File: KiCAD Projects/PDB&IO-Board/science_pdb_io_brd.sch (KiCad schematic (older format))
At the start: 21 parts, among them P1 ROBOT_PWR_IN, P12 ENCODER_2, P13 LIMIT1_IN, P14 LIMIT2_IN, P15 LIMIT3_IN, P16 ENCODER_3, P17 MOTOR1_PWM, P18 MOTOR2_PWM, P19 MOTOR3_PWM, P2 12V-5V_REG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

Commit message: More schematic work
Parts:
- added C? (x3): C, symbol C
- added R? (x3): R, symbol R
- added U?: SN74HC14N, symbol SN74HC14N
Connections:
- net +5V: now also R?.1, R?.1, R?.1, U?.14 (Vcc)
- net GND: now also C?.2, C?.2, C?.2, U?.7 (GND)
- net LIMIT1_IN: now also U?.2 (1Y); no longer P13.2 (P2)
- net LIMIT2_IN: now also U?.4; no longer P14.2 (P2)
- net LIMIT3_IN: now also U?.6 (3Y); no longer P15.2 (P2)
- new net B_LIM1: C?.1, P13.2 (P2), R?.2, U?.1 (1A)
- new net B_LIM2: C?.1, P14.2 (P2), R?.2, U?.3 (2A)
- new net B_LIM3: C?.1, P15.2 (P2), R?.2, U?.5 (3A)
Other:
- moved on the sheet: P13, P14, P15, P17, P18, P19, P20

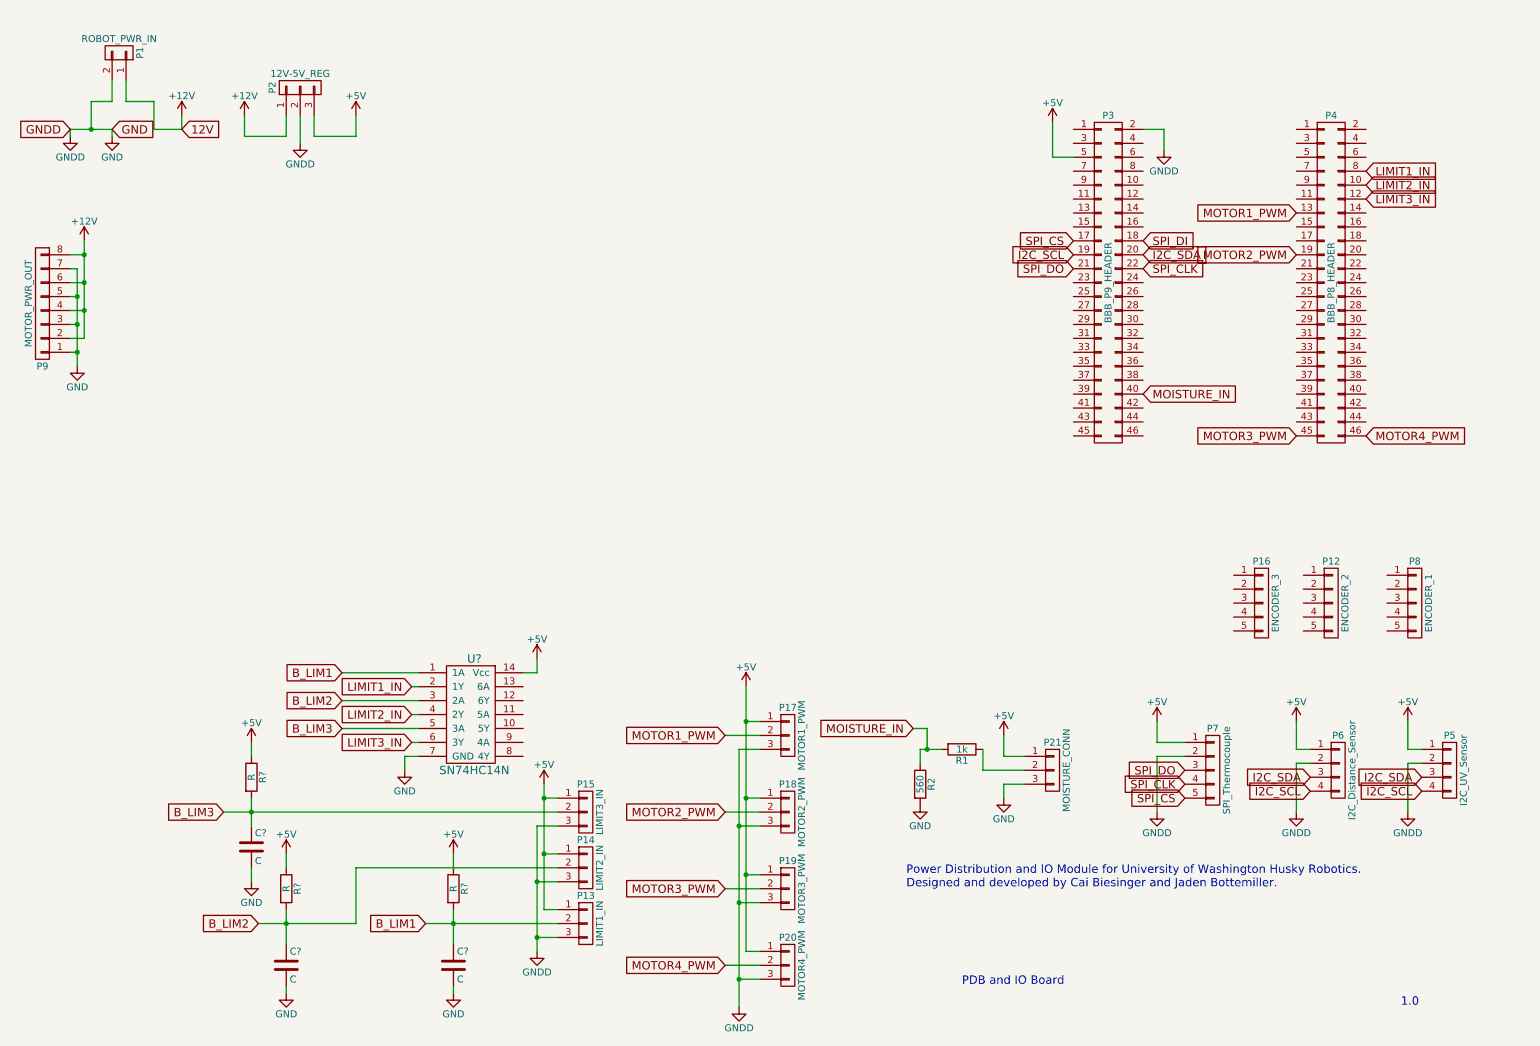
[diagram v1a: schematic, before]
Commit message: Minor Schematic Tweaks
No functional changes, just making the schematic look a little nicer.
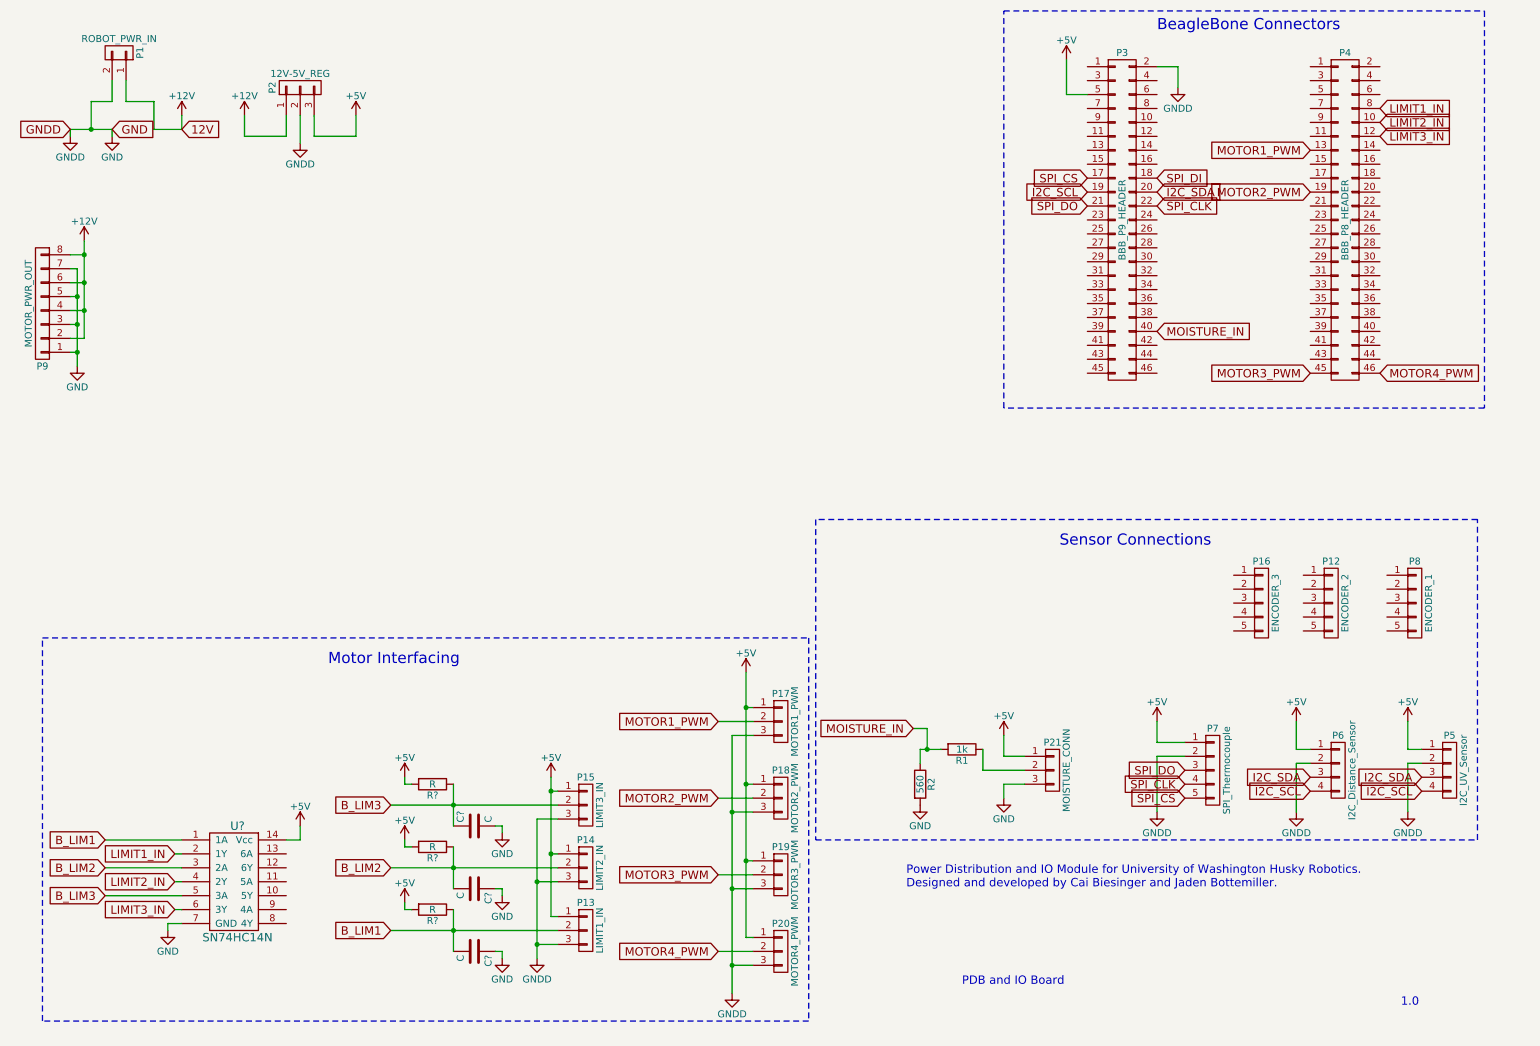
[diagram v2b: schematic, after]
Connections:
- net +5V: now also R?.2, R?.2, R?.2; no longer R?.1, R?.1, R?.1
- net B_LIM1: now also C?.2, R?.1; no longer C?.1, R?.2
- net B_LIM2: now also C?.2, R?.1; no longer C?.1, R?.2
- net B_LIM3: now also R?.1; no longer R?.2
- net GND: now also C?.1, C?.1; no longer C?.2, C?.2
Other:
- note added: "BeagleBone Connectors"
- note added: "Motor Interfacing"
- note added: "Sensor Connections"
- moved on the sheet: C?, P13, P15, P17, P18, P19, P20, P3, P4, R?, U?

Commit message: Board updates
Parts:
- added P?: BB_Power, symbol CONN_01X02
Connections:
- net +5V: now also P?.2 (P2); no longer P3.5 (P5)
- net GND: now also P?.1 (P1); no longer P3.2 (P2)
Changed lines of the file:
@@
 	1    0    0    -1
 $EndComp
-Text GLabel 1050 1350 0    60   Input ~ 0
-GNDD
-Text GLabel 1350 1350 2    60   Input ~ 0
-GND
 $Comp
 L +12V #PWR5
@@
 	1    0    0    -1
 $EndComp
-Text GLabel 1850 1350 2    60   Input ~ 0
-12V
 $Comp
 L CONN_01X02 P1
@@
 	1    0    0    -1
 $EndComp
-$Comp
-L +5V #PWR16
-U 1 1 5891B3C4
-P 8200 850
-F 0 "#PWR16" H 8200 700 50  0001 C CNN
-F 1 "+5V" H 8200 990 50  0000 C CNN
-F 2 "" H 8200 850 50  0000 C CNN
-F 3 "" H 8200 850 50  0000 C CNN
-	1    8200 850
-	1    0    0    -1
-$EndComp
-$Comp
-L GNDD #PWR19
-U 1 1 5891B4A8
-P 9000 1050
-F 0 "#PWR19" H 9000 800 50  0001 C CNN
-F 1 "GNDD" H 9000 900 50  0000 C CNN
-F 2 "" H 9000 1050 50  0000 C CNN
-F 3 "" H 9000 1050 50  0000 C CNN
-	1    9000 1050
-	1    0    0    -1
-$EndComp
 Text GLabel 10450 1200 2    60   Input ~ 0
 LIMIT1_IN
@@
 	7150 5800 7150 5900
 Wire Wire Line
-	7150 5800 7300 5800
+	7150 5800 7200 5800
+Wire Wire Line
+	7200 5800 7300 5800
 Wire Wire Line
 	7600 5950 7900 5950
@@
 	5800 5700 5950 5700
 Wire Wire Line
-	5800 5700 5800 7550
+	5800 5700 5800 6250
+Wire Wire Line
+	5800 6250 5800 6800
+Wire Wire Line
+	5800 6800 5800 7350
+Wire Wire Line
+	5800 7350 5800 7550
 Wire Wire Line
 	5900 7150 5950 7150
 Wire Wire Line
-	5900 5250 5900 7150
-Wire Wire Line
-	9000 900  9000 1050
-Wire Wire Line
-	8850 900  9000 900
-Wire Wire Line
-	8200 1100 8350 1100
-Wire Wire Line
-	8200 850  8200 1100
-Wire Wire Line
-	3350 6200 4550 6200
-Wire Wire Line
-	3350 7100 4550 7100
+	5900 5250 5900 5500
+Wire Wire Line
+	5900 5500 5900 6050
+Wire Wire Line
+	5900 6050 5900 6600
+Wire Wire Line
+	5900 6600 5900 7150
+Wire Wire Line
+	3350 6200 3800 6200
+Wire Wire Line
+	3800 6200 4550 6200
+Wire Wire Line
+	3350 7100 3800 7100
+Wire Wire Line
+	3800 7100 4550 7100
 Connection ~ 4400 7200
 Wire Wire Line
@@
 	4500 7000 4550 7000
 Wire Wire Line
-	4500 6000 4500 7000
+	4500 6000 4500 6100
+Wire Wire Line
+	4500 6100 4500 6550
+Wire Wire Line
+	4500 6550 4500 7000
 Wire Wire Line
 	4400 6300 4550 6300
 Wire Wire Line
-	4400 6300 4400 7300
+	4400 6300 4400 6750
+Wire Wire Line
+	4400 6750 4400 7200
+Wire Wire Line
+	4400 7200 4400 7300
 Connection ~ 1150 2450
 Wire Wire Line
@@
 	1150 2850 1050 2850
 Wire Wire Line
-	1150 2150 1150 2850
+	1150 2150 1150 2250
+Wire Wire Line
+	1150 2250 1150 2450
+Wire Wire Line
+	1150 2450 1150 2650
+Wire Wire Line
+	1150 2650 1150 2850
 Wire Wire Line
 	1050 2250 1150 2250
@@
 	1050 2550 1100 2550
 Wire Wire Line
-	1100 2350 1100 3050
+	1100 2350 1100 2550
+Wire Wire Line
+	1100 2550 1100 2750
+Wire Wire Line
+	1100 2750 1100 2950
+Wire Wire Line
+	1100 2950 1100 3050
 Wire Wire Line
 	1050 2350 1100 2350
@@
 	1350 1350 1350 1400
 Wire Wire Line
-	1050 1350 1350 1350
+	1050 1350 1200 1350
+Wire Wire Line
+	1200 1350 1350 1350
 Wire Wire Line
 	1050 1400 1050 1350
@@
 $EndComp
 Wire Wire Line
-	3800 6500 3800 6800
+	3800 6500 3800 6650
+Wire Wire Line
+	3800 6650 3800 6800
 $Comp
 L R R?
@@
 $EndComp
 Wire Wire Line
-	3800 6950 3800 7250
+	3800 6950 3800 7100
+Wire Wire Line
+	3800 7100 3800 7250
 $Comp
 L C C?
@@
 	4150 6800 4100 6800
 Wire Wire Line
-	3350 6650 4550 6650
+	3350 6650 3800 6650
+Wire Wire Line
+	3800 6650 4550 6650
 Connection ~ 3800 6650
 Wire Wire Line
-	3800 6050 3800 6350
+	3800 6050 3800 6200
+Wire Wire Line
+	3800 6200 3800 6350
 Wire Wire Line
 	4150 6400 4150 6350
@@
 Text Notes 2900 5200 0    80   ~ 0
 Motor Interfacing
+$Comp
+L CONN_01X02 P?
+U 1 1 58A8DADF
+P 1600 2000
+F 0 "P?" H 1600 2150 50  0000 C CNN
+F 1 "BB_Power" V 1700 2000 50  0000 C CNN
+F 2 "" H 1600 2000 50  0000 C CNN
+F 3 "" H 1600 2000 50  0000 C CNN
+	1    1600 2000
+	-1   0    0    1
+$EndComp
+Wire Wire Line
+	1800 1950 1900 1950
+Wire Wire Line
+	1900 1950 1900 1850
+Wire Wire Line
+	1800 2050 1900 2050
+Wire Wire Line
+	1900 2050 1900 2150
+$Comp
+L +5V #PWR?
+U 1 1 58A8EB99
+P 1900 1850
+F 0 "#PWR?" H 1900 1700 50  0001 C CNN
+F 1 "+5V" H 1900 1990 50  0000 C CNN
+F 2 "" H 1900 1850 50  0000 C CNN
+F 3 "" H 1900 1850 50  0000 C CNN
+	1    1900 1850
+	1    0    0    -1
+$EndComp
+$Comp
+L GNDD #PWR?
+U 1 1 58A8EBE7
+P 1900 2150
+F 0 "#PWR?" H 1900 1900 50  0001 C CNN
+F 1 "GNDD" H 1900 2000 50  0000 C CNN
+F 2 "" H 1900 2150 50  0000 C CNN
+F 3 "" H 1900 2150 50  0000 C CNN
+	1    1900 2150
+	1    0    0    -1
+$EndComp
 $EndSCHEMATC

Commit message: Fixed pinouts, started board layout.
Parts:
- removed P5: I2C_UV_Sensor, symbol CONN_01X04
- removed P6: I2C_Distance_Sensor, symbol CONN_01X04
- removed P7: SPI_Thermocouple, symbol CONN_01X05
- added P?: CONN_01X07, symbol CONN_01X07
- added P?: CONN_01X05, symbol CONN_01X05
- added P?: CONN_01X06, symbol CONN_01X06
- gave numbers to parts that had none: 8
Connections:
- net +5V: now also P?.1 (P1), P?.1 (P1), P?.2 (P2)
- net GND: now also P3.1 (P1), P3.2 (P2), P3.43 (P43), P3.44 (P44), P3.45 (P45), P3.46 (P46), P4.1 (P1), P4.2 (P2), P?.2 (P2), P?.3 (P3), P?.3 (P3); no longer P21.3 (P3), R2.2
- net I2C_SCL: now also P?.3 (P3), P?.5 (P5)
- net I2C_SDA: now also P?.4 (P4), P?.4 (P4)
- net SPI_CLK: now also P?.6 (P6)
- net SPI_CS: now also P?.5 (P5)
- net SPI_DO: now also P?.4 (P4)
- net GNDA: now reaches P3.34 (P34)
- net GNDA: now also P21.3 (P3), R2.2
- no-connect marks 0 -> 5
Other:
- moved on the sheet: R2

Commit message: Worked on PCB
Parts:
- P3, P4: footprint (none) -> Pin_Headers:Pin_Header_Straight_2x23_Pitch2.54mm
- P5: renamed from P?; footprint (none) -> Pin_Headers:Pin_Header_Straight_1x06_Pitch2.54mm
- P6: renamed from P?; footprint (none) -> Pin_Headers:Pin_Header_Straight_1x07_Pitch2.54mm
- P7: renamed from P?; footprint (none) -> Pin_Headers:Pin_Header_Straight_1x05_Pitch2.54mm
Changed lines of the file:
@@
 F 0 "P1" H 1400 950 50  0000 C CNN
 F 1 "ROBOT_PWR_IN" V 1500 800 50  0000 C CNN
-F 2 "" H 1400 800 50  0000 C CNN
+F 2 "" H 1400 800 50  0001 C CNN
 F 3 "" H 1400 800 50  0000 C CNN
 	1    1400 800
@@
 F 0 "P2" H 2700 1250 50  0000 C CNN
 F 1 "12V-5V_REG" V 2800 1050 50  0000 C CNN
-F 2 "" H 2700 1050 50  0000 C CNN
+F 2 "" H 2700 1050 50  0001 C CNN
 F 3 "" H 2700 1050 50  0000 C CNN
 	1    2700 1050
@@
 F 0 "P3" H 8600 3200 50  0000 C CNN
 F 1 "BBB_P9_HEADER" V 8600 2000 50  0000 C CNN
-F 2 "" H 8600 1150 50  0000 C CNN
+F 2 "Pin_Headers:Pin_Header_Straight_2x23_Pitch2.54mm" H 8600 1150 50  0001 C CNN
 F 3 "" H 8600 1150 50  0000 C CNN
 	1    8600 2000
@@
 F 0 "P4" H 10200 3200 50  0000 C CNN
 F 1 "BBB_P8_HEADER" V 10200 2000 50  0000 C CNN
-F 2 "" H 10200 1150 50  0000 C CNN
+F 2 "Pin_Headers:Pin_Header_Straight_2x23_Pitch2.54mm" H 10200 1150 50  0001 C CNN
 F 3 "" H 10200 1150 50  0000 C CNN
 	1    10200 2000
@@
 F 0 "P9" H 850 3050 50  0000 C CNN
 F 1 "MOTOR_PWR_OUT" V 950 2600 50  0000 C CNN
-F 2 "" H 850 2600 50  0000 C CNN
+F 2 "" H 850 2600 50  0001 C CNN
 F 3 "" H 850 2600 50  0000 C CNN
 	1    850  2600
@@
 F 0 "P8" H 10700 5050 50  0000 C CNN
 F 1 "ENCODER_1" V 10800 4750 50  0000 C CNN
-F 2 "" H 10700 4750 50  0000 C CNN
+F 2 "" H 10700 4750 50  0001 C CNN
 F 3 "" H 10700 4750 50  0000 C CNN
 	1    10700 4750
@@
 F 0 "P12" H 10100 5050 50  0000 C CNN
 F 1 "ENCODER_2" V 10200 4750 50  0000 C CNN
-F 2 "" H 10100 4750 50  0000 C CNN
+F 2 "" H 10100 4750 50  0001 C CNN
 F 3 "" H 10100 4750 50  0000 C CNN
 	1    10100 4750
@@
 F 0 "P15" H 4750 6400 50  0000 C CNN
 F 1 "LIMIT3_IN" V 4850 6200 50  0000 C CNN
-F 2 "" H 4750 6200 50  0000 C CNN
+F 2 "" H 4750 6200 50  0001 C CNN
 F 3 "" H 4750 6200 50  0000 C CNN
 	1    4750 6200
@@
 F 0 "P14" H 4750 6850 50  0000 C CNN
 F 1 "LIMIT2_IN" V 4850 6650 50  0000 C CNN
-F 2 "" H 4750 6650 50  0000 C CNN
+F 2 "" H 4750 6650 50  0001 C CNN
 F 3 "" H 4750 6650 50  0000 C CNN
 	1    4750 6650
@@
 F 0 "P13" H 4750 7300 50  0000 C CNN
 F 1 "LIMIT1_IN" V 4850 7100 50  0000 C CNN
-F 2 "" H 4750 7100 50  0000 C CNN
+F 2 "" H 4750 7100 50  0001 C CNN
 F 3 "" H 4750 7100 50  0000 C CNN
 	1    4750 7100
@@
 F 0 "P16" H 9600 5050 50  0000 C CNN
 F 1 "ENCODER_3" V 9700 4750 50  0000 C CNN
-F 2 "" H 9600 4750 50  0000 C CNN
+F 2 "" H 9600 4750 50  0001 C CNN
 F 3 "" H 9600 4750 50  0000 C CNN
 	1    9600 4750
@@
 F 0 "P20" H 6150 7450 50  0000 C CNN
 F 1 "MOTOR4_PWM" V 6250 7250 50  0000 C CNN
-F 2 "" H 6150 7250 50  0000 C CNN
+F 2 "" H 6150 7250 50  0001 C CNN
 F 3 "" H 6150 7250 50  0000 C CNN
 	1    6150 7250
@@
 F 0 "P19" H 6150 6900 50  0000 C CNN
 F 1 "MOTOR3_PWM" V 6250 6700 50  0000 C CNN
-F 2 "" H 6150 6700 50  0000 C CNN
+F 2 "" H 6150 6700 50  0001 C CNN
 F 3 "" H 6150 6700 50  0000 C CNN
 	1    6150 6700
@@
 F 0 "P18" H 6150 6350 50  0000 C CNN
 F 1 "MOTOR2_PWM" V 6250 6150 50  0000 C CNN
-F 2 "" H 6150 6150 50  0000 C CNN
+F 2 "" H 6150 6150 50  0001 C CNN
 F 3 "" H 6150 6150 50  0000 C CNN
 	1    6150 6150
@@
 F 0 "P17" H 6150 5800 50  0000 C CNN
 F 1 "MOTOR1_PWM" V 6250 5600 50  0000 C CNN
-F 2 "" H 6150 5600 50  0000 C CNN
+F 2 "" H 6150 5600 50  0001 C CNN
 F 3 "" H 6150 5600 50  0000 C CNN
 	1    6150 5600
@@
 F 0 "P21" H 8100 6150 50  0000 C CNN
 F 1 "MOISTURE_CONN" V 8200 5950 50  0000 C CNN
-F 2 "" H 8100 5950 50  0000 C CNN
+F 2 "" H 8100 5950 50  0001 C CNN
 F 3 "" H 8100 5950 50  0000 C CNN
 	1    8100 5950
@@
 F 0 "R1" V 7530 5800 50  0000 C CNN
 F 1 "1k" V 7450 5800 50  0000 C CNN
-F 2 "" V 7380 5800 50  0000 C CNN
+F 2 "" V 7380 5800 50  0001 C CNN
 F 3 "" H 7450 5800 50  0000 C CNN
 	1    7450 5800
@@
 F 0 "R2" V 7280 6050 50  0000 C CNN
 F 1 "560" V 7200 6050 50  0000 C CNN
-F 2 "" V 7130 6050 50  0000 C CNN
+F 2 "" V 7130 6050 50  0001 C CNN
 F 3 "" H 7200 6050 50  0000 C CNN
 	1    7200 6050
@@
 F 0 "R3" V 3730 6050 50  0000 C CNN
 F 1 "R" V 3650 6050 50  0000 C CNN
-F 2 "" V 3580 6050 50  0000 C CNN
+F 2 "" V 3580 6050 50  0001 C CNN
 F 3 "" H 3650 6050 50  0000 C CNN
 	1    3650 6050
@@
 F 0 "C1" H 3975 6450 50  0000 L CNN
 F 1 "C" H 3975 6250 50  0000 L CNN
-F 2 "" H 3988 6200 50  0000 C CNN
+F 2 "" H 3988 6200 50  0001 C CNN
 F 3 "" H 3950 6350 50  0000 C CNN
 	1    3950 6350
@@
 F 0 "R4" V 3730 6500 50  0000 C CNN
 F 1 "R" V 3650 6500 50  0000 C CNN
-F 2 "" V 3580 6500 50  0000 C CNN
+F 2 "" V 3580 6500 50  0001 C CNN
 F 3 "" H 3650 6500 50  0000 C CNN
 	1    3650 6500
@@
 F 0 "C2" H 3975 6900 50  0000 L CNN
 F 1 "C" H 3975 6700 50  0000 L CNN
-F 2 "" H 3988 6650 50  0000 C CNN
+F 2 "" H 3988 6650 50  0001 C CNN
 F 3 "" H 3950 6800 50  0000 C CNN
 	1    3950 6800
@@
 F 0 "R5" V 3730 6950 50  0000 C CNN
 F 1 "R" V 3650 6950 50  0000 C CNN
-F 2 "" V 3580 6950 50  0000 C CNN
+F 2 "" V 3580 6950 50  0001 C CNN
 F 3 "" H 3650 6950 50  0000 C CNN
 	1    3650 6950
@@
 F 0 "C3" H 3975 7350 50  0000 L CNN
 F 1 "C" H 3975 7150 50  0000 L CNN
-F 2 "" H 3988 7100 50  0000 C CNN
+F 2 "" H 3988 7100 50  0001 C CNN
 F 3 "" H 3950 7250 50  0000 C CNN
 	1    3950 7250
@@
 F 0 "P10" H 1600 2150 50  0000 C CNN
 F 1 "BB_Power" V 1700 2000 50  0000 C CNN
-F 2 "" H 1600 2000 50  0000 C CNN
+F 2 "" H 1600 2000 50  0001 C CNN
 F 3 "" H 1600 2000 50  0000 C CNN
 	1    1600 2000
@@
 	9750 900  9750 950
 $Comp
-L CONN_01X07 P?
+L CONN_01X07 P6
 U 1 1 58B25587
 P 10100 5850
-F 0 "P?" H 10100 6250 50  0000 C CNN
+F 0 "P6" H 10100 6250 50  0000 C CNN
 F 1 "CONN_01X07" V 10200 5850 50  0000 C CNN
-F 2 "" H 10100 5850 50  0000 C CNN
+F 2 "Pin_Headers:Pin_Header_Straight_1x07_Pitch2.54mm" H 10100 5850 50  0001 C CNN
 F 3 "" H 10100 5850 50  0000 C CNN
 	1    10100 5850
@@
 NoConn ~ 9900 5550
 $Comp
-L CONN_01X05 P?
+L CONN_01X05 P7
 U 1 1 58B28A2C
 P 11000 5950
-F 0 "P?" H 11000 6250 50  0000 C CNN
+F 0 "P7" H 11000 6250 50  0000 C CNN
 F 1 "CONN_01X05" V 11100 5950 50  0000 C CNN
-F 2 "" H 11000 5950 50  0000 C CNN
+F 2 "Pin_Headers:Pin_Header_Straight_1x05_Pitch2.54mm" H 11000 5950 50  0001 C CNN
 F 3 "" H 11000 5950 50  0000 C CNN
 	1    11000 5950
@@
 NoConn ~ 10800 6150
 $Comp
-L CONN_01X06 P?
+L CONN_01X06 P5
 U 1 1 58B2A688
 P 9200 5900
-F 0 "P?" H 9200 6250 50  0000 C CNN
+F 0 "P5" H 9200 6250 50  0000 C CNN
 F 1 "CONN_01X06" V 9300 5900 50  0000 C CNN
-F 2 "" H 9200 5900 50  0000 C CNN
+F 2 "Pin_Headers:Pin_Header_Straight_1x06_Pitch2.54mm" H 9200 5900 50  0001 C CNN
 F 3 "" H 9200 5900 50  0000 C CNN
 	1    9200 5900

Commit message: Added Pullup Resistors to Encoder Channels
Needs to look more pretty
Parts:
- removed P12: ENCODER_2, symbol CONN_01X05
- removed P8: ENCODER_1, symbol CONN_01X05
- added P?: ENCODER_1, symbol CONN_01X05
- added P?: ENCODER_2, symbol CONN_01X05
- added R? (x9): R, symbol R
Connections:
- net +5V: now also P16.1 (P1), P?.1 (P1), P?.1 (P1), R?.1, R?.1, R?.1, R?.1, R?.1, R?.1, R?.1, R?.1, R?.1
- net GND: now also P16.5 (P5), P?.5 (P5), P?.5 (P5)
- net ENC3_A: now reaches P16.2 (P2)
- net ENC3_B: now reaches P16.3 (P3)
- net ENC3_B: now also R?.2, R?.2
- net ENC3_BUT: now reaches P16.4 (P4)
- net ENC3_BUT: now also R?.2
- new net ENC1_A: P?.2 (P2)
- new net ENC1_B: P?.3 (P3), R?.2, R?.2
- new net ENC1_BUT: P?.4 (P4), R?.2
- new net ENC2_A: P?.2 (P2)
- new net ENC2_B: P?.3 (P3), R?.2, R?.2
- new net ENC2_BUT: P?.4 (P4), R?.2
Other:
- moved on the sheet: P16

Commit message: Created Better Pullup resistors
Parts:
- removed R? (x8): R, symbol R
- added R? (x8): 5k, symbol R
- R?: value R -> 5k
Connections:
- net +5V: now also R?.1, R?.1, R?.1, R?.1, R?.1, R?.1, R?.1, R?.1
- net ENC1_A: now also R?.2
- net ENC1_B: now also R?.2
- net ENC1_BUT: now also R?.2
- net ENC2_A: now also R?.2
- net ENC2_B: now also R?.2; no longer R?.2
- net ENC2_BUT: now also R?.2
- net ENC3_A: now also R?.2
- net ENC3_B: now also R?.2
- net ENC3_BUT: now also R?.2
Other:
- moved on the sheet: P16, P?, R?

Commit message: Made temp values for RC LPF. Updated components
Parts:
- C1, C2, C3: value C -> 1u
- R3, R4, R5: value R -> 5k
- gave numbers to parts that had none: 11
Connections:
- net B_LIM3: now also C1.2; no longer C1.1
- net GND: now also C1.1; no longer C1.2
